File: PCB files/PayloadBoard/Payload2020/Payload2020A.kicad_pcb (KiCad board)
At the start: 2 copper layers, 50 x 152 mm, 3 parts, among them U1 Teensy3.6, U2 ArduCam, U3 HX711_Breakout

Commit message: Board A changes from previous commit, mis-click
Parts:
- added C1: 1uF, Capacitor_SMD:C_1206_3216Metric, F.Cu at (95.1, 77.9)
- added C2: 1uF, Capacitor_SMD:C_1206_3216Metric, F.Cu at (106.7, 77.7)
- added C3: 10uF, Capacitor_SMD:C_1206_3216Metric, F.Cu at (82.2, 69.7)
- added C4: 10uF, Capacitor_SMD:C_1206_3216Metric, F.Cu at (87.8, 69.7)
- added J1: BATTERY, Connector_JST:JST_EH_S2B-EH_1x02_P2.50mm_Horizontal, F.Cu at (115.6, 72.5)
- added L1: 2.2uH, Inductor_SMD:L_1210_3225Metric, F.Cu at (93.4, 70.2)
- added U4: AP7370-50W5-7, Package_TO_SOT_SMD:SOT-23-5, F.Cu at (101.6, 77.6)
- added U5: TPS613222ADBVR, Package_TO_SOT_SMD:SOT-23-5, F.Cu at (101.5, 70.4)
- moved U3 60.2 mm to (104.5, 170.7), turned to 0 degrees
- moved U1 16.2 mm to (99.3, 117.6)
- moved U2 9.02 mm to (100.2, 44.2), turned to 180 degrees
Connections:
- net Net-(U1-Pad16) renamed /XBEE_RTS
- net Net-(U1-Pad17) renamed /XBEE_CTS
- net Net-(U1-Pad18) renamed /TX_GPS
- net Net-(U1-Pad19) renamed /RX_GPS
- net Net-(U1-Pad20) renamed /XBEE_DOUT
- net Net-(U1-Pad21) renamed /XBEE_DIN
- net Net-(U1-Pad5) renamed /Berry_SCL
- net Net-(U1-Pad6) renamed /Berry_SDA
- U1 pad 11: Net-(U1-Pad11) -> /Ardu_CS
- U1 pad 13: Net-(U1-Pad13) -> /Ardu_MOSI
- U1 pad 14: Net-(U1-Pad14) -> /Ardu_MISO
- U1 pad 15: +3V3 -> Net-(U1-Pad15)
- U1 pad 2: Net-(U1-Pad2) -> /HX_OUT
- U1 pad 3: Net-(U1-Pad3) -> /HX_CLK
- U1 pad 40: Net-(U1-Pad40) -> /Ardu_SCK
- U1 pad 45: /SDA0 -> /Ardu_SCL
- U1 pad 46: /SCL0 -> /Ardu_SDA
- U1 pad 51: +3V3 -> Net-(U1-Pad51)
- U1 pad 53: Net-(U1-Pad53) -> +5V
- U2 pad 1: Net-(U2-Pad1) -> /Ardu_CS
- U2 pad 2: Net-(U2-Pad2) -> /Ardu_MOSI
- U2 pad 3: Net-(U2-Pad3) -> /Ardu_MISO
- U2 pad 4: Net-(U2-Pad4) -> /Ardu_SCK
- U2 pad 7: /SDA0 -> Net-(U1-Pad35)
- U2 pad 8: /SCL0 -> Net-(U1-Pad34)
- U3 pad 10: (no net) -> +3V3
- U3 pad 7: (no net) -> GNDREF
- U3 pad 8: (no net) -> /HX_OUT
- U3 pad 9: (no net) -> /HX_CLK

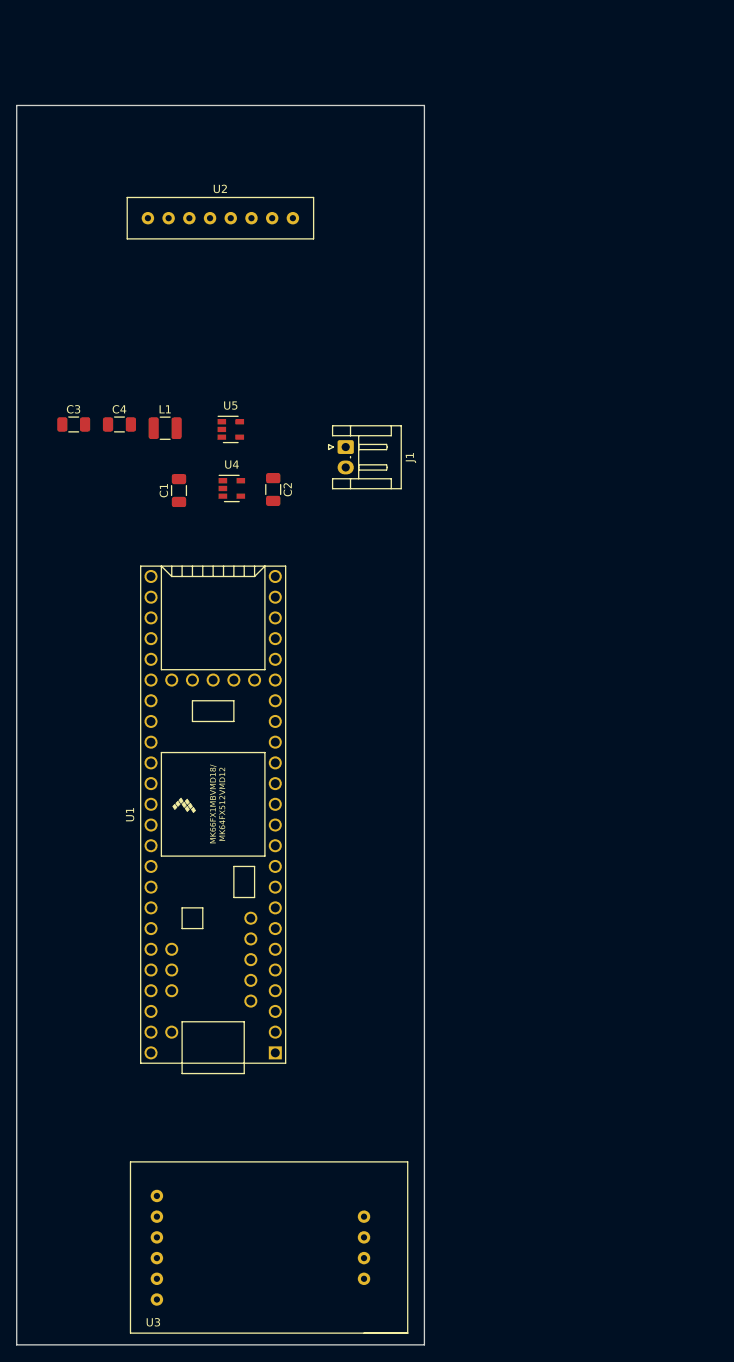
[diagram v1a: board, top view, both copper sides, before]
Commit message: Changed board sizes based on payload bay dimensions Changed battery connector to JST XH
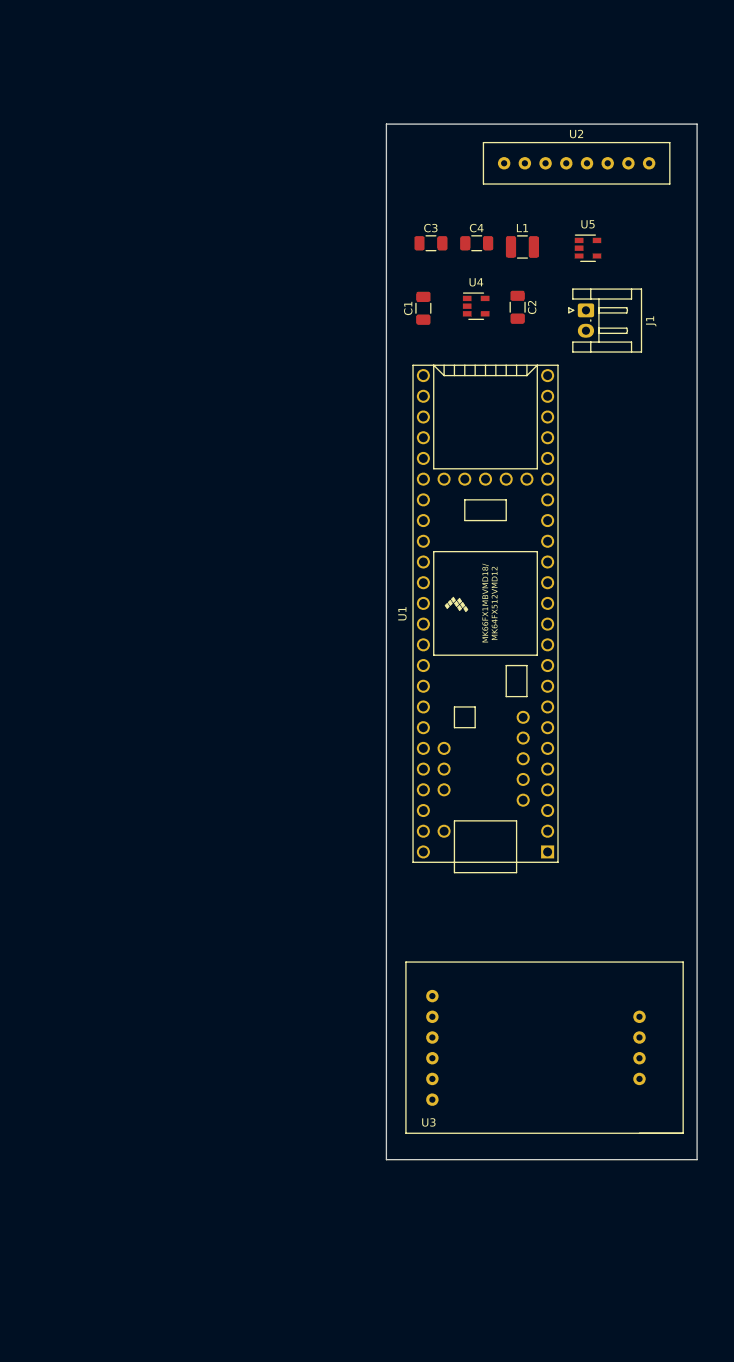
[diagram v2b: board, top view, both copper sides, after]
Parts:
- moved U5 49.1 mm to (145.3, 48.1)
- moved L1 49.1 mm to (137.2, 48.0)
- moved C3 49.1 mm to (126.0, 47.5)
- moved C4 49.1 mm to (131.6, 47.5)
- moved U2 44.2 mm to (143.9, 37.5)
- moved U3 41.7 mm to (138.3, 146.2)
- moved U1 41.5 mm to (132.7, 93.0)
- moved U4 37.4 mm to (131.6, 55.2)
- moved C1 37.4 mm to (125.1, 55.5)
- moved C2 37.4 mm to (136.7, 55.4)
- moved J1 33.9 mm to (145.0, 55.8)
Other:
- board size 50 x 152 mm -> 38.1 x 127 mm
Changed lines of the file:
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@@
   )
   (module teensy:Teensy35_36 (layer F.Cu)
-    (at 99.314 117.602 90)
+    (at 132.715 92.964 90)
     (fp_text reference U1 (at 0 -10.16 90) (layer F.SilkS)
       (effects (font (size 1 1) (thickness 0.15)))
@@
   )
   (module Payload:ArduCam (layer F.Cu)
-    (at 100.203 44.196 180)
+    (at 143.891 37.465 180)
     (fp_text reference U2 (at 0 3.302) (layer F.SilkS)
       (effects (font (size 1 1) (thickness 0.15)))
@@
   )
   (module Capacitor_SMD:C_1206_3216Metric (layer F.Cu)
-    (at 95.123 77.851 90)
+    (at 125.095 55.499 90)
     (descr "Capacitor SMD 1206 (3216 Metric), square (rectangular) end terminal, IPC_7351 nominal, (Body size source: http://www.tortai-tech.com/upload/download/2011102023233369053.pdf), generated with kicad-footprint-generator")
     (tags capacitor)
@@
   )
   (module Capacitor_SMD:C_1206_3216Metric (layer F.Cu)
-    (at 106.68 77.724 270)
+    (at 136.652 55.372 270)
     (descr "Capacitor SMD 1206 (3216 Metric), square (rectangular) end terminal, IPC_7351 nominal, (Body size source: http://www.tortai-tech.com/upload/download/2011102023233369053.pdf), generated with kicad-footprint-generator")
     (tags capacitor)
@@
   )
   (module Capacitor_SMD:C_1206_3216Metric (layer F.Cu)
-    (at 82.210001 69.747001)
+    (at 126.025001 47.522001)
     (descr "Capacitor SMD 1206 (3216 Metric), square (rectangular) end terminal, IPC_7351 nominal, (Body size source: http://www.tortai-tech.com/upload/download/2011102023233369053.pdf), generated with kicad-footprint-generator")
     (tags capacitor)
@@
   )
   (module Capacitor_SMD:C_1206_3216Metric (layer F.Cu)
-    (at 87.820001 69.747001)
+    (at 131.635001 47.522001)
     (descr "Capacitor SMD 1206 (3216 Metric), square (rectangular) end terminal, IPC_7351 nominal, (Body size source: http://www.tortai-tech.com/upload/download/2011102023233369053.pdf), generated with kicad-footprint-generator")
     (tags capacitor)
@@
   )
   (module Connector_JST:JST_EH_S2B-EH_1x02_P2.50mm_Horizontal (layer F.Cu)
-    (at 115.57 72.517 270)
+    (at 145.034 55.753 270)
     (descr "JST EH series connector, S2B-EH (http://www.jst-mfg.com/product/pdf/eng/eEH.pdf), generated with kicad-footprint-generator")
     (tags "connector JST EH horizontal")
@@
   )
   (module Inductor_SMD:L_1210_3225Metric (layer F.Cu)
-    (at 93.430001 70.207001)
+    (at 137.245001 47.982001)
     (descr "Inductor SMD 1210 (3225 Metric), square (rectangular) end terminal, IPC_7351 nominal, (Body size source: http://www.tortai-tech.com/upload/download/2011102023233369053.pdf), generated with kicad-footprint-generator")
     (tags inductor)
@@
   )
   (module Payload:HX711_Breakout (layer F.Cu)
-    (at 104.521 170.688)
+    (at 138.303 146.177)
     (fp_text reference U3 (at -12.54252 9.20496) (layer F.SilkS)
       (effects (font (size 1 1) (thickness 0.15)))
@@
   )
   (module Package_TO_SOT_SMD:SOT-23-5 (layer F.Cu)
-    (at 101.6 77.597)
+    (at 131.572 55.245)
     (descr "5-pin SOT23 package")
     (tags SOT-23-5)
@@
   )
   (module Package_TO_SOT_SMD:SOT-23-5 (layer F.Cu)
-    (at 101.473 70.358)
+    (at 145.288 48.133)
     (descr "5-pin SOT23 package")
     (tags SOT-23-5)
@@
     )
   )
-  (gr_text "TOP of BAY" (at 100.076 25.019) (layer Dwgs.User)
+  (gr_text "TOP of BAY" (at 145.415 27.305) (layer Dwgs.User)
     (effects (font (size 5 5) (thickness 0.15)))
   )
-  (gr_line (start 75.222 30.626) (end 125.222 30.626) (layer Edge.Cuts) (width 0.1))
-  (gr_line (start 75.222 30.626) (end 75.222 182.626) (layer Edge.Cuts) (width 0.1))
-  (gr_line (start 125.222 30.626) (end 125.222 182.626) (layer Edge.Cuts) (width 0.1))
-  (gr_line (start 75.222 182.626) (end 125.222 182.626) (layer Edge.Cuts) (width 0.1))
+  (gr_line (start 120.561 32.912) (end 158.661 32.912) (layer Edge.Cuts) (width 0.1))
+  (gr_line (start 120.561 32.912) (end 120.561 159.912) (layer Edge.Cuts) (width 0.1))
+  (gr_line (start 158.661 32.912) (end 158.661 159.912) (layer Edge.Cuts) (width 0.1))
+  (gr_line (start 120.561 159.912) (end 158.661 159.912) (layer Edge.Cuts) (width 0.1))
 )

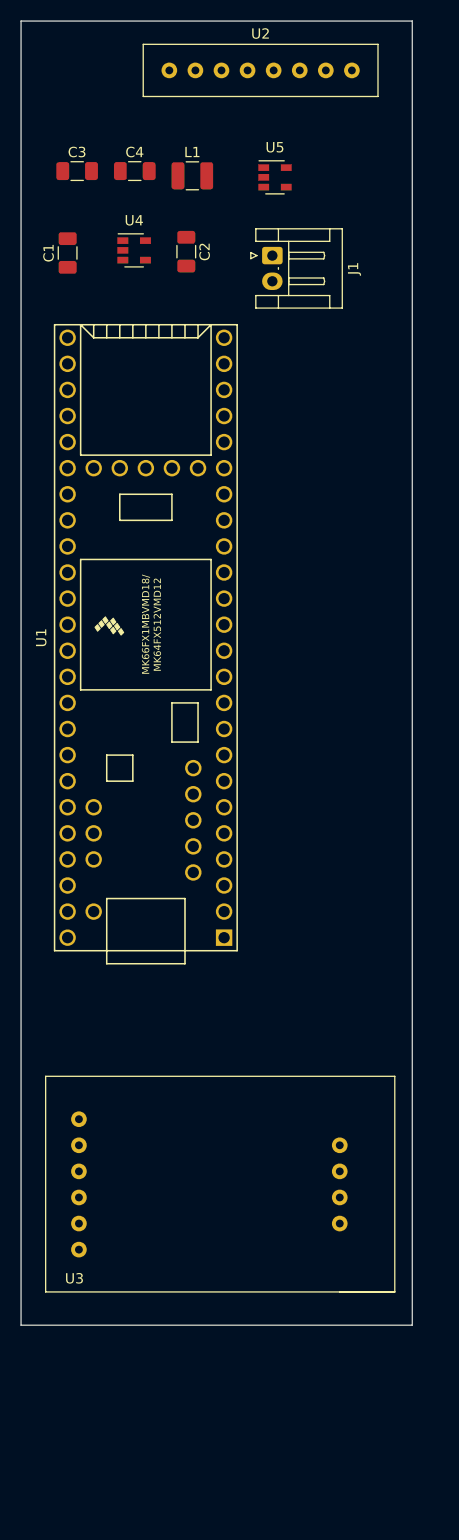
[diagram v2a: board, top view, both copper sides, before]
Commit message: -Selected all footprints -Began routing Board A
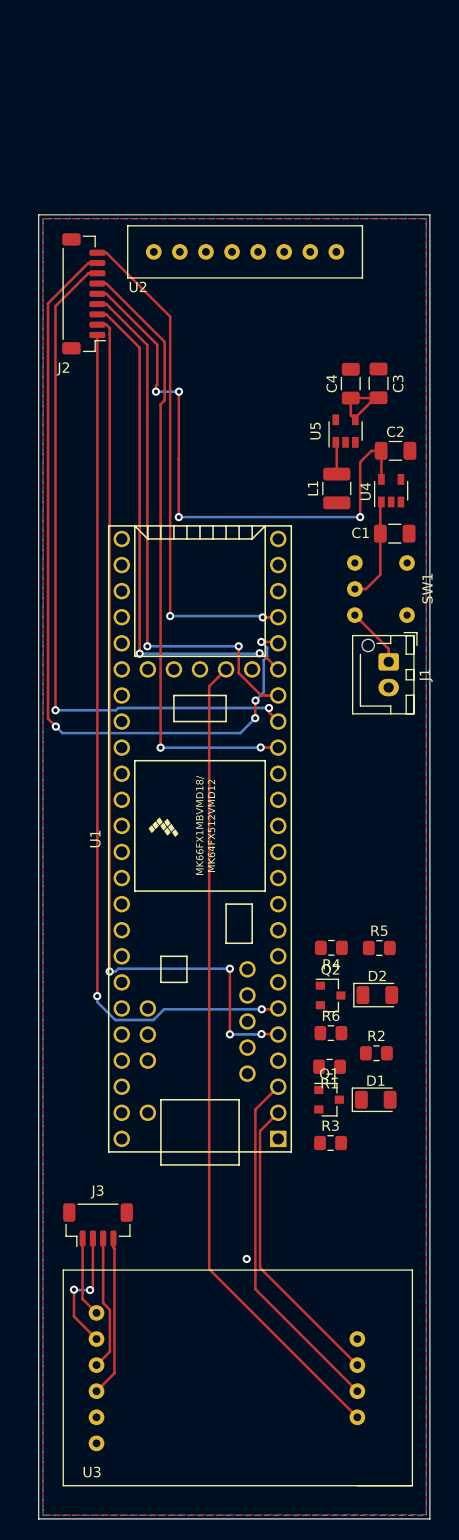
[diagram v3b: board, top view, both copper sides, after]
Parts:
- added D1: LED, LED_SMD:LED_1206_3216Metric, F.Cu at (155.1, 138.0)
- added D2: LED, LED_SMD:LED_1206_3216Metric, F.Cu at (155.3, 127.8)
- added J2: BridgeConn, Connector_JST:JST_SH_BM09B-SRSS-TB_1x09-1MP_P1.00mm_Vertical, F.Cu at (126.7, 59.5)
- added J3: LoadCell, Connector_JST:JST_SH_BM04B-SRSS-TB_1x04-1MP_P1.00mm_Vertical, F.Cu at (128.1, 150.1)
- added Q1: Q_NMOS_GSD, Package_TO_SOT_SMD:SOT-23, F.Cu at (150.6, 137.9)
- added Q2: Q_NMOS_GSD, Package_TO_SOT_SMD:SOT-23, F.Cu at (150.7, 127.8)
- added R1: 1k, Resistor_SMD:R_0805_2012Metric_Pad1.15x1.40mm_HandSolder, F.Cu at (150.6, 134.7)
- added R2: 100k, Resistor_SMD:R_0805_2012Metric_Pad1.15x1.40mm_HandSolder, F.Cu at (155.2, 133.4)
- added R3: 100, Resistor_SMD:R_0805_2012Metric_Pad1.15x1.40mm_HandSolder, F.Cu at (150.7, 142.2)
- added R4: 10k, Resistor_SMD:R_0805_2012Metric_Pad1.15x1.40mm_HandSolder, F.Cu at (150.8, 123.2)
- added R5: 10k, Resistor_SMD:R_0805_2012Metric_Pad1.15x1.40mm_HandSolder, F.Cu at (155.5, 123.2)
- added R6: 100, Resistor_SMD:R_0805_2012Metric_Pad1.15x1.40mm_HandSolder, F.Cu at (150.7, 131.5)
- added SW1: SW_SPST, Payload:GW12RCH, F.Cu at (156.0, 88.2)
- J1: footprint Connector_JST:JST_EH_S2B-EH_1x02_P2.50mm_Horizontal -> Connector_JST:JST_XH_B2B-XH-AM_1x02_P2.50mm_Vertical
- moved C1 42.0 mm to (156.9, 82.8), turned to 180 degrees
- moved J1 41.2 mm to (156.4, 95.3)
- moved C3 35.9 mm to (155.4, 68.2), turned to 90 degrees
- moved U4 34.3 mm to (156.6, 78.6), turned to 90 degrees
- moved L1 33.5 mm to (151.3, 78.4), turned to 90 degrees
- moved C4 29.5 mm to (152.7, 68.2), turned to 90 degrees
- moved C2 28.1 mm to (157.0, 74.8), turned to 0 degrees
- moved U5 25.6 mm to (152.2, 72.8), turned to 90 degrees
- moved U1 20.3 mm to (138.0, 112.6)
- moved U3 18.9 mm to (140.0, 165.0)
- moved U2 17.7 mm to (142.4, 55.1)
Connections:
- J1 pad 1: Net-(C1-Pad2) -> Net-(J1-Pad1)
- U1 pad 4: Net-(U1-Pad4) -> /USR_LED1
- U1 pad 8: Net-(U1-Pad8) -> /USR_LED2
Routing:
- net /Berry_SCL: track 0.00 -> 87.0 mm, vias 0 -> 4
- net /Berry_SDA: track 0.00 -> 83.8 mm, vias 0 -> 2
- net +3V3: track 0.00 -> 79.5 mm
- net /XBEE_DOUT: track 0.00 -> 78.1 mm, vias 0 -> 4
- net /XBEE_CTS: track 0.00 -> 67.3 mm, vias 0 -> 2
- net /XBEE_RTS: track 0.00 -> 60.1 mm, vias 0 -> 2
- net +3.3VA: track 0.00 -> 55.3 mm, vias 0 -> 4
- net /TX_GPS: track 0.00 -> 52.1 mm, vias 0 -> 2
- net /RX_GPS: track 0.00 -> 49.4 mm, vias 0 -> 2
- net /XBEE_DIN: track 0.00 -> 49.4 mm, vias 0 -> 2
- net /HX_CLK: track 0.00 -> 34.7 mm
- net /HX_OUT: track 0.00 -> 29.2 mm
- net Net-(J3-Pad4): track 0.00 -> 15.6 mm
- net Net-(J3-Pad3): track 0.00 -> 13.1 mm
- net Net-(J3-Pad2): track 0.00 -> 12.4 mm, vias 0 -> 2
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- added copper zone on B.Cu, net GNDREF
- added copper zone on F.Cu, net GNDREF
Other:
- board text added: "BACK - Horizontal FRONT - Vertical"
